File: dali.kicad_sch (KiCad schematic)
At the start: 13 parts, among them J2 Screw_Terminal_01x02, J26 Screw_Terminal_01x02, J27 Screw_Terminal_01x02, Q2 MMBT2222A, U1 TCLT1000, U2 TCLT1000

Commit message: Assign footprints to resistors and use solder jumpers
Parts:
- R4, R5, R6, R7, R8: footprint (none) -> Resistor_SMD:R_0805_2012Metric_Pad1.20x1.40mm_HandSolder
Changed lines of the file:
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@@
 			)
 		)
-		(property "Footprint" ""
+		(property "Footprint" "Resistor_SMD:R_0805_2012Metric_Pad1.20x1.40mm_HandSolder"
 			(at 154.432 49.53 90)
 			(effects
@@
 			)
 		)
-		(property "Footprint" ""
+		(property "Footprint" "Resistor_SMD:R_0805_2012Metric_Pad1.20x1.40mm_HandSolder"
 			(at 84.582 48.26 90)
 			(effects
@@
 			)
 		)
-		(property "Footprint" ""
+		(property "Footprint" "Resistor_SMD:R_0805_2012Metric_Pad1.20x1.40mm_HandSolder"
 			(at 54.102 48.26 90)
 			(effects
@@
 			)
 		)
-		(property "Footprint" ""
+		(property "Footprint" "Resistor_SMD:R_0805_2012Metric_Pad1.20x1.40mm_HandSolder"
 			(at 137.16 43.688 90)
 			(effects
@@
 			)
 		)
-		(property "Footprint" ""
+		(property "Footprint" "Resistor_SMD:R_0805_2012Metric_Pad1.20x1.40mm_HandSolder"
 			(at 185.42 28.448 90)
 			(effects

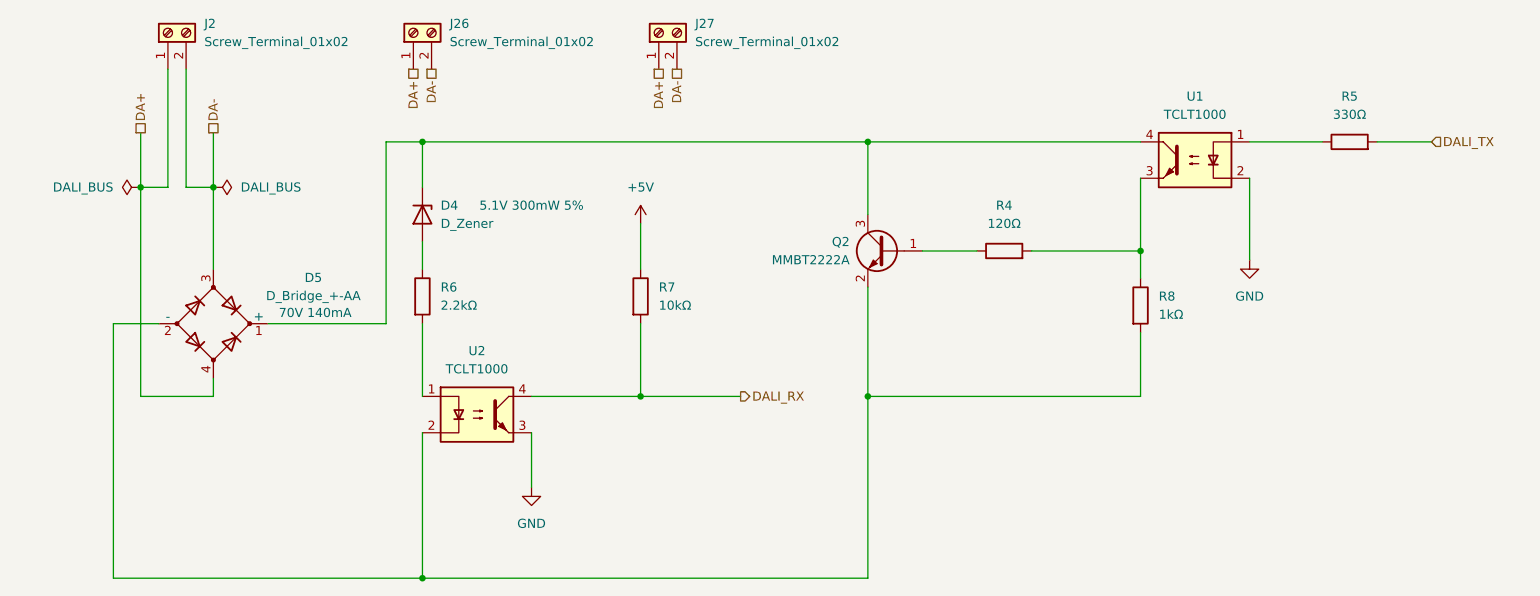
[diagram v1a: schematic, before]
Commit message: Assign footprints for the remaining components
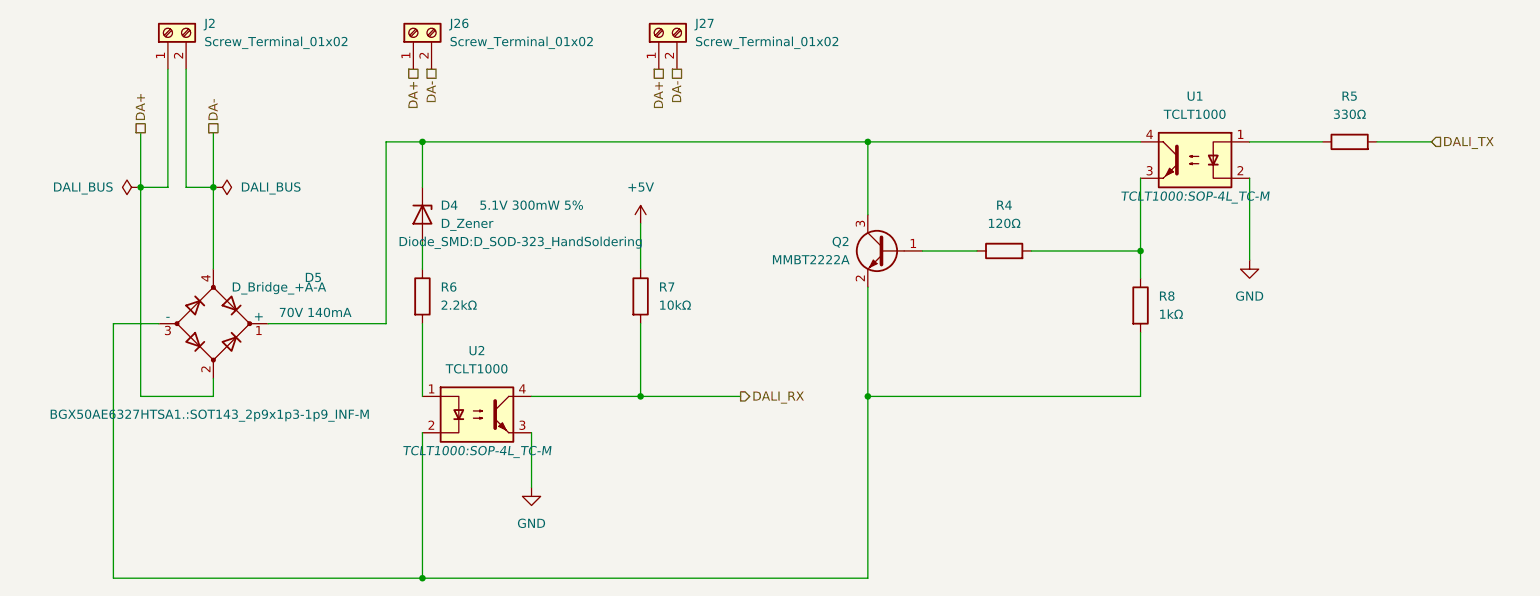
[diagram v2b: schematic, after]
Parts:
- D4: footprint (none) -> Diode_SMD:D_SOD-323_HandSoldering
- D5: value D_Bridge_+-AA -> D_Bridge_+A-A; footprint (none) -> BGX50AE6327HTSA1.:SOT143_2p9x1p3-1p9_INF-M; symbol Device:D_Bridge_+-AA -> Device:D_Bridge_+A-A
- J2, J26, J27: footprint (none) -> TerminalBlock:TerminalBlock_bornier-2_P5.08mm
- U1, U2: footprint TCLT1000:SOP-4L_TC -> TCLT1000:SOP-4L_TC-M
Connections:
- net DA+: now also D5.2; no longer D5.4
- net DA-: now also D5.4; no longer D5.3
- net at Q2.2 (E), R8.2, U2.2: now also D5.3 (-); no longer D5.2 (-)
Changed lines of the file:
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@@
 			)
 		)
-		(property "Footprint" ""
+		(property "Footprint" "TerminalBlock:TerminalBlock_bornier-2_P5.08mm"
 			(at 20.32 11.43 0)
 			(effects
@@
 			)
 		)
-		(property "Footprint" ""
+		(property "Footprint" "TerminalBlock:TerminalBlock_bornier-2_P5.08mm"
 			(at 88.9 11.43 0)
 			(effects
@@
 	)
 	(symbol
-		(lib_id "Device:D_Bridge_+-AA")
+		(lib_id "Device:D_Bridge_+A-A")
 		(at 26.67 52.07 0)
 		(unit 1)
@@
 			)
 		)
-		(property "Value" "D_Bridge_+-AA"
-			(at 40.64 48.1898 0)
-			(effects
-				(font
-					(size 1.27 1.27)
-				)
-			)
-		)
-		(property "Footprint" ""
-			(at 26.67 52.07 0)
-			(effects
-				(font
-					(size 1.27 1.27)
-				)
-				(hide yes)
+		(property "Value" "D_Bridge_+A-A"
+			(at 29.21 46.99 0)
+			(effects
+				(font
+					(size 1.27 1.27)
+				)
+				(justify left)
+			)
+		)
+		(property "Footprint" "BGX50AE6327HTSA1.:SOT143_2p9x1p3-1p9_INF-M"
+			(at 26.162 64.77 0)
+			(effects
+				(font
+					(size 1.27 1.27)
+				)
 			)
 		)
@@
 			)
 		)
-		(property "Description" "Diode bridge, +ve/-ve/AC/AC"
+		(property "Description" "Diode bridge, +ve/AC/-ve/AC"
 			(at 26.67 52.07 0)
 			(effects
@@
 			)
 		)
-		(property "Footprint" "TCLT1000:SOP-4L_TC"
+		(property "Footprint" "TCLT1000:SOP-4L_TC-M"
 			(at 163.83 34.29 0)
 			(effects
@@
 					(italic yes)
 				)
-				(hide yes)
 			)
 		)
@@
 			)
 		)
-		(property "Footprint" "TCLT1000:SOP-4L_TC"
+		(property "Footprint" "TCLT1000:SOP-4L_TC-M"
 			(at 63.5 69.85 0)
 			(effects
@@
 					(italic yes)
 				)
-				(hide yes)
 			)
 		)
@@
 			)
 		)
-		(property "Footprint" ""
+		(property "Footprint" "TerminalBlock:TerminalBlock_bornier-2_P5.08mm"
 			(at 54.61 11.43 0)
 			(effects
@@
 			)
 		)
-		(property "Footprint" ""
-			(at 55.88 36.83 0)
-			(effects
-				(font
-					(size 1.27 1.27)
-				)
-				(hide yes)
-			)
-		)
+		(property "Footprint" "Diode_SMD:D_SOD-323_HandSoldering"
+			(at 69.596 40.64 90)
+			(effects
+				(font
+					(size 1.27 1.27)
+				)
+			)
+		)

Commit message: Update schematic for 3.3V and specify resistor power
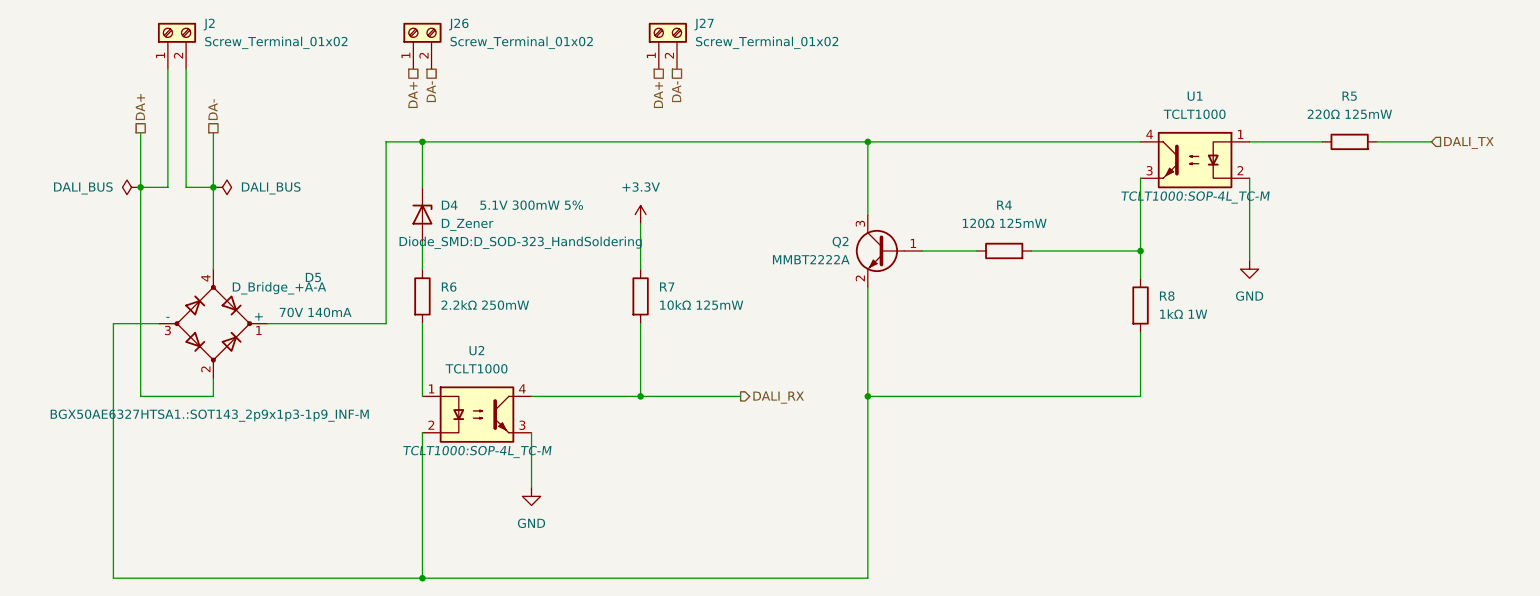
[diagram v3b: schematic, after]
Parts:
- R4: value 120Ω -> 120Ω 125mW
- R5: value 330Ω -> 220Ω 125mW
- R6: value 2.2kΩ -> 2.2kΩ 250mW
- R7: value 10kΩ -> 10kΩ 125mW
- R8: value 1kΩ -> 1kΩ 1W
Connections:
- net +5V renamed +3.3V
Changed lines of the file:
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@@
 			)
 		)
-		(property "Value" "1kΩ"
+		(property "Value" "1kΩ 1W"
 			(at 158.75 50.7999 0)
 			(effects
@@
 			)
 		)
-		(property "Value" "10kΩ"
+		(property "Value" "10kΩ 125mW"
 			(at 88.9 49.5299 0)
 			(effects
@@
 			)
 		)
-		(property "Value" "+5V"
+		(property "Value" "+3.3V"
 			(at 86.36 33.02 0)
 			(effects
@@
 			)
 		)
-		(property "Description" "Power symbol creates a global label with name \"+5V\""
+		(property "Description" "Power symbol creates a global label with name \"+3.3V\""
 			(at 86.36 38.1 0)
 			(effects
@@
 			)
 		)
-		(property "Value" "2.2kΩ"
+		(property "Value" "2.2kΩ 250mW"
 			(at 58.42 49.5299 0)
 			(effects
@@
 			)
 		)
-		(property "Value" "120Ω"
+		(property "Value" "120Ω 125mW"
 			(at 137.16 38.1 90)
 			(effects
@@
 			)
 		)
-		(property "Value" "330Ω"
+		(property "Value" "220Ω 125mW"
 			(at 185.42 22.86 90)
 			(effects

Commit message: Place all components
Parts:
- J15: renamed from J26; value Screw_Terminal_01x02 -> DALI BUS
- J16: renamed from J27; value Screw_Terminal_01x02 -> DALI BUS
- J2: value Screw_Terminal_01x02 -> DALI BUS
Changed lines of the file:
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@@
 			)
 		)
-		(property "Value" "Screw_Terminal_01x02"
+		(property "Value" "DALI BUS"
 			(at 25.4 12.6999 90)
 			(effects
@@
 		(dnp no)
 		(fields_autoplaced yes)
-		(property "Reference" "J27"
+		(property "Reference" "J16"
 			(at 93.98 10.1599 90)
 			(effects
@@
 			)
 		)
-		(property "Value" "Screw_Terminal_01x02"
+		(property "Value" "DALI BUS"
 			(at 93.98 12.6999 90)
 			(effects
@@
 			(project "dali-pcb"
 				(path "/aa7f7e07-1f39-4222-a272-c9975d033b6d/da3e6e2b-6a82-47d9-9b10-47b7831d6589"
-					(reference "J27")
+					(reference "J16")
 					(unit 1)
 				)
@@
 		(dnp no)
 		(fields_autoplaced yes)
-		(property "Reference" "J26"
+		(property "Reference" "J15"
 			(at 59.69 10.1599 90)
 			(effects
@@
 			)
 		)
-		(property "Value" "Screw_Terminal_01x02"
+		(property "Value" "DALI BUS"
 			(at 59.69 12.6999 90)
 			(effects
@@
 			(project "dali-pcb"
 				(path "/aa7f7e07-1f39-4222-a272-c9975d033b6d/da3e6e2b-6a82-47d9-9b10-47b7831d6589"
-					(reference "J26")
-					(unit 1)
-				)
+					(reference "J15")
+					(unit 1)
+				)

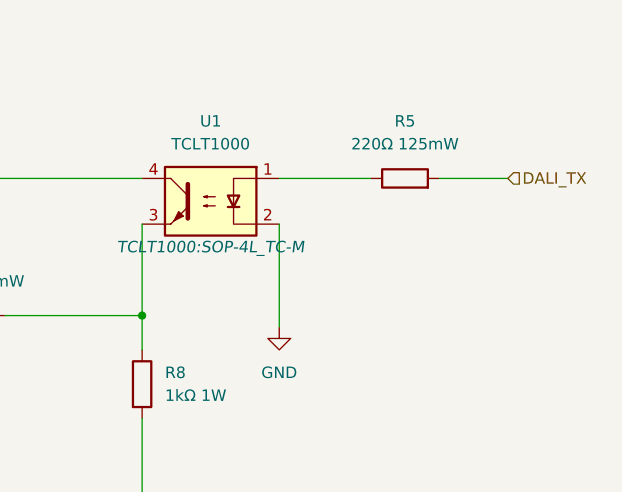
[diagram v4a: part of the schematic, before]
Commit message: FTDI TTL-232R-3V3 can't be used to directly interface with DALI
There's no 3.3V supply to use as a pull-up
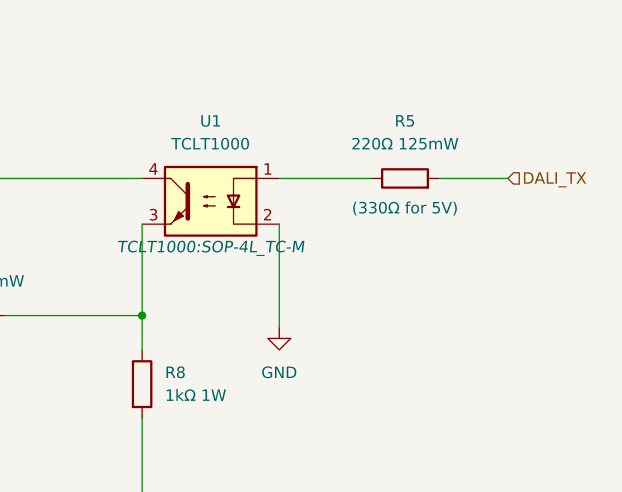
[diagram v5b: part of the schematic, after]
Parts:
- R5: Note (none) -> (330Ω for 5V)
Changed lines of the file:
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@@
 		(on_board yes)
 		(dnp no)
-		(fields_autoplaced yes)
 		(property "Reference" "R5"
 			(at 185.42 20.32 90)
@@
 			)
 		)
+		(property "Note" "(330Ω for 5V)"
+			(at 185.42 29.972 90)
+			(effects
+				(font
+					(size 1.27 1.27)
+				)
+			)
+		)

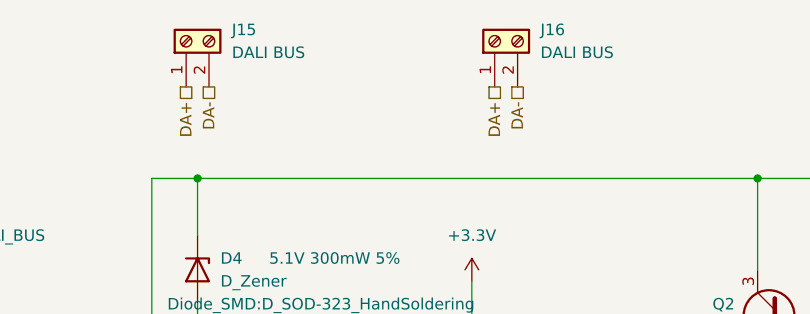
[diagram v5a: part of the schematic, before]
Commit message: Renumber references and place LOLIN-S3-MINI
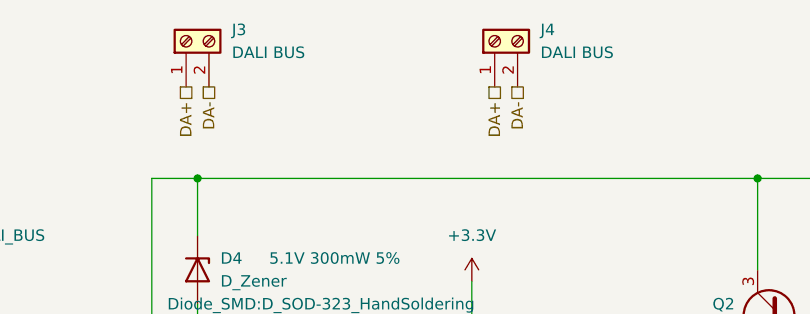
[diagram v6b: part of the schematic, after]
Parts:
- renumbered J15 to J3, J16 to J4
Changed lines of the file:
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@@
 		(dnp no)
 		(fields_autoplaced yes)
-		(property "Reference" "J16"
+		(property "Reference" "J4"
 			(at 93.98 10.1599 90)
 			(effects
@@
 			(project "dali-pcb"
 				(path "/aa7f7e07-1f39-4222-a272-c9975d033b6d/da3e6e2b-6a82-47d9-9b10-47b7831d6589"
-					(reference "J16")
+					(reference "J4")
 					(unit 1)
 				)
@@
 		(dnp no)
 		(fields_autoplaced yes)
-		(property "Reference" "J15"
+		(property "Reference" "J3"
 			(at 59.69 10.1599 90)
 			(effects
@@
 			(project "dali-pcb"
 				(path "/aa7f7e07-1f39-4222-a272-c9975d033b6d/da3e6e2b-6a82-47d9-9b10-47b7831d6589"
-					(reference "J15")
-					(unit 1)
-				)
+					(reference "J3")
+					(unit 1)
+				)

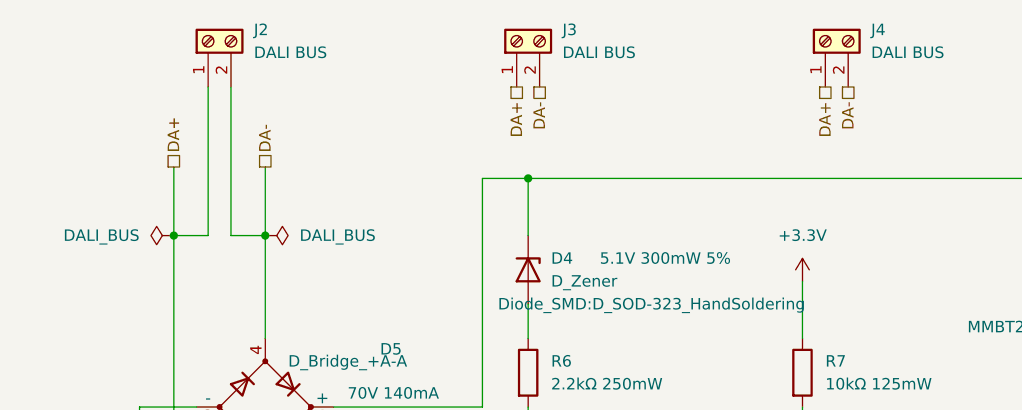
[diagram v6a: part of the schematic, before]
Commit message: Fix screw terminal orientation and mounting holes
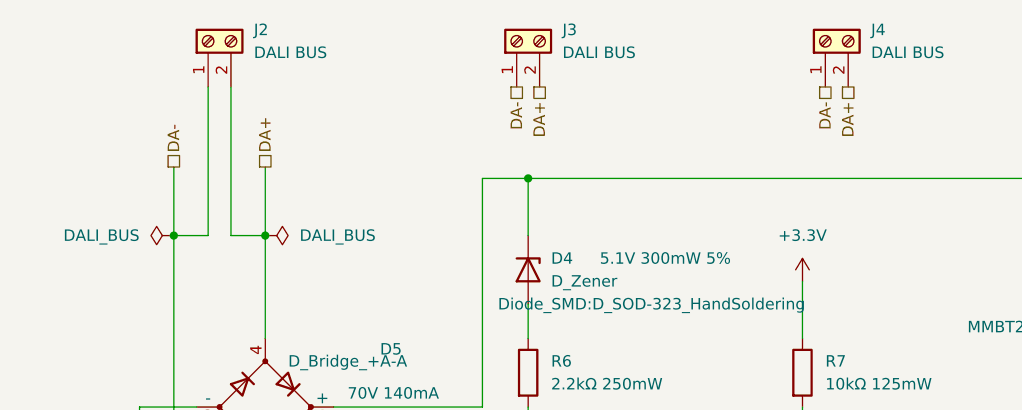
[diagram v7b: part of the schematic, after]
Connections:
- net DA+: now also D5.4, J2.2 (Pin_2), J3.2 (Pin_2), J4.2 (Pin_2); no longer D5.2, J2.1 (Pin_1), J3.1 (Pin_1), J4.1 (Pin_1)
- net DA-: now also D5.2, J2.1 (Pin_1), J3.1 (Pin_1), J4.1 (Pin_1); no longer D5.4, J2.2 (Pin_2), J3.2 (Pin_2), J4.2 (Pin_2)
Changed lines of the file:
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@@
 	(hierarchical_label "DA-"
 		(shape passive)
-		(at 57.15 16.51 270)
+		(at 54.61 16.51 270)
 		(effects
 			(font
@@
 	(hierarchical_label "DA-"
 		(shape passive)
-		(at 26.67 25.4 90)
+		(at 16.51 25.4 90)
 		(effects
 			(font
@@
 	(hierarchical_label "DA-"
 		(shape passive)
-		(at 91.44 16.51 270)
+		(at 88.9 16.51 270)
 		(effects
 			(font
@@
 	(hierarchical_label "DA+"
 		(shape passive)
-		(at 54.61 16.51 270)
+		(at 57.15 16.51 270)
 		(effects
 			(font
@@
 	(hierarchical_label "DA+"
 		(shape passive)
-		(at 88.9 16.51 270)
+		(at 91.44 16.51 270)
 		(effects
 			(font
@@
 	(hierarchical_label "DA+"
 		(shape passive)
-		(at 16.51 25.4 90)
+		(at 26.67 25.4 90)
 		(effects
 			(font

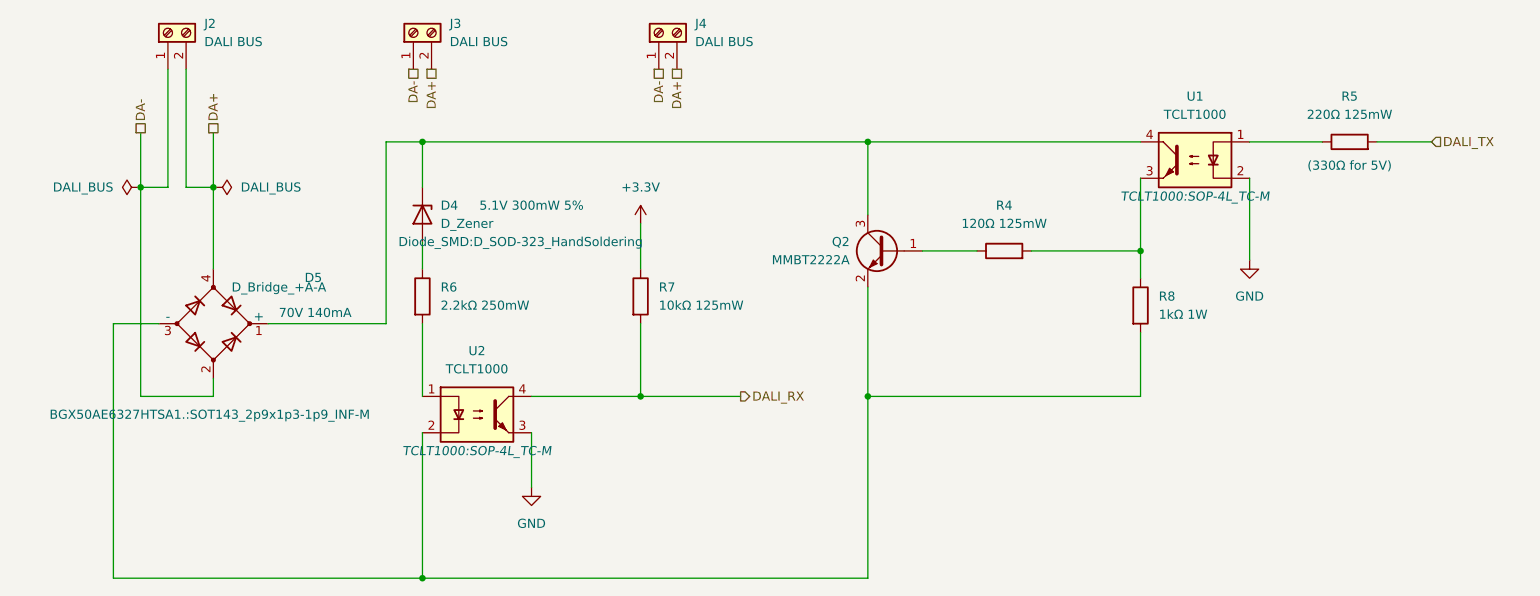
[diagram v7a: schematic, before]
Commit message: Add solder jumpers to bypass the bridge rectifier
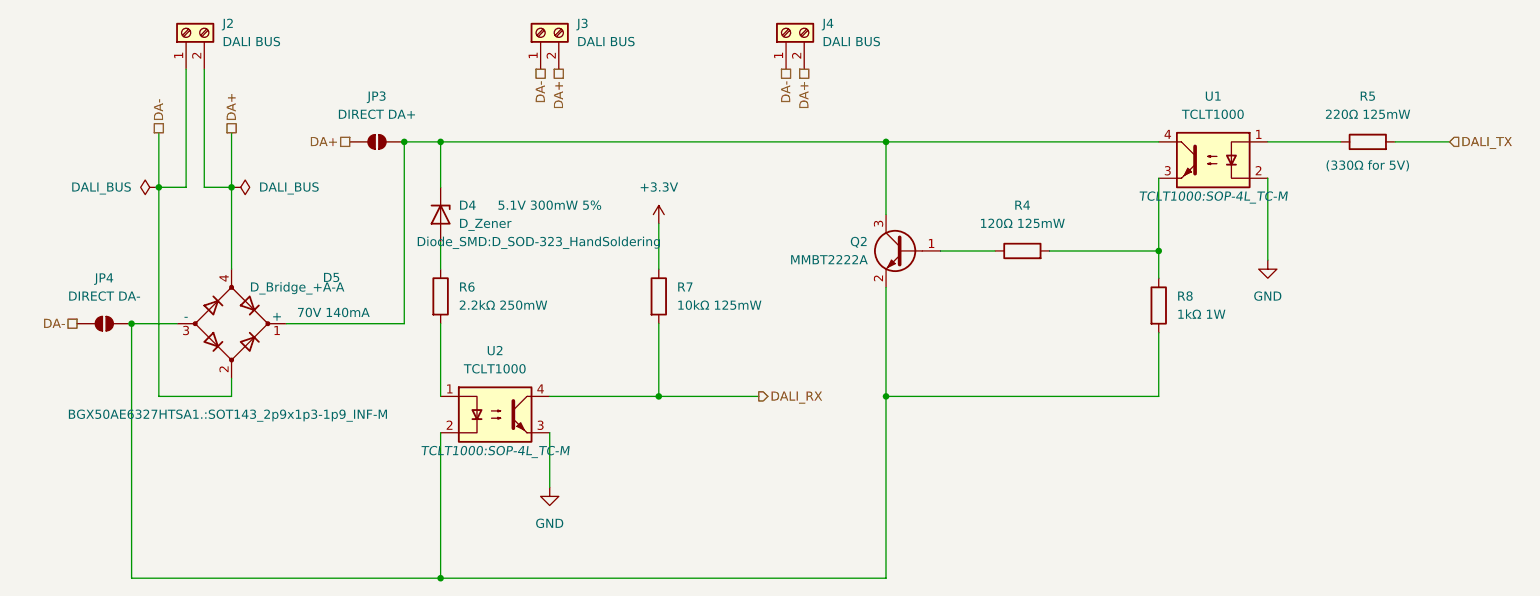
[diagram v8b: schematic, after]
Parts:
- added JP3: DIRECT DA+, Jumper:SolderJumper-2_P1.3mm_Open_RoundedPad1.0x1.5mm, symbol Jumper:SolderJumper_2_Open
- added JP4: DIRECT DA-, Jumper:SolderJumper-2_P1.3mm_Open_RoundedPad1.0x1.5mm, symbol Jumper:SolderJumper_2_Open
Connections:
- net DA+: now also JP3.2 (B)
- net DA-: now also JP4.2 (B)
- net at D5.3 (-), Q2.2 (E), R8.2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: now also JP4.1 (A)
- net at D4.1 (K), D5.1 (+), Q2.3 (C)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: now also JP3.1 (A)
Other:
- moved on the sheet: D4, D5, J2, J3, J4, Q2, R4, R5, R6, R7, R8, U1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
